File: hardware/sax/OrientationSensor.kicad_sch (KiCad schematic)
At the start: 9 parts, among them U1401 BMM150, U1402 BHI160

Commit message: Update library
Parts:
- C1401: footprint Capacitor_SMD:C_0603_1608Metric -> V2_Capacitor_SMD:C_0603; symbol Device:C_Small -> V2_Device:C_0603_10u; Manufacturer (none) -> TDK; Mouser (none) -> 810-C1608X6S1A106M; Product (none) -> C1608X6S1A106M080AC
- C1403: footprint Capacitor_SMD:C_0603_1608Metric -> V2_Capacitor_SMD:C_0603; symbol Device:C_Small -> V2_Device:C_0603_0u1; Manufacturer (none) -> TDK; Mouser (none) -> 810-CGA3E2X7R1H104MA; Product (none) -> CGA3E2X7R1H104M080AA
- C1404: footprint Capacitor_SMD:C_0603_1608Metric -> V2_Capacitor_SMD:C_0603; symbol Device:C_Small -> V2_Device:C_0603_0u47; Manufacturer (none) -> YAGEO; Mouser (none) -> 603-CC0603JR6BB474; Product (none) -> CC0603JRX7R6BB474
- R1402, R1403, R1405, R1406: footprint Resistor_SMD:R_0603_1608Metric -> V2_Resistor_SMD:R_0603; symbol Device:R_Small -> V2_Device:R_0603_2k7; Manufacturer (none) -> Vishay; Mouser (none) -> 71-CRCW06032K70FKEAC; Product (none) -> CRCW06032K70FKEAC; Rating (none) -> 100mW
- U1401: LCSC (none) -> C171681; Manufacturer (none) -> Bosch; Product (none) -> BMM150
- U1402: LCSC (none) -> C464452; Manufacturer (none) -> Bosch; Product (none) -> BHI160B
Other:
- moved on the sheet: R1402, R1403

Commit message: Replace Order_Number
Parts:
- C1401: Rating (none) -> 10V
- C1403: Rating (none) -> 50V
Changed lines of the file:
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@@
+			)
+		)
+		(property "Rating" "10V"
+			(at 130.81 113.03 0)
+			(effects
+				(font
+					(size 1.27 1.27)
+				)
+				(hide yes)
 			)
 		)
@@
 			)
 		)
-		(property "Description" "Power symbol creates a global label with name \"+3V3\""
+		(property "Description" ""
 			(at 95.25 91.44 0)
 			(effects
@@
 			)
 		)
-		(property "Description" "Power symbol creates a global label with name \"+3V3\""
+		(property "Description" ""
 			(at 125.73 85.09 0)
 			(effects
@@
 			)
 		)
-		(property "Description" "Power symbol creates a global label with name \"GND\" , ground"
+		(property "Description" ""
 			(at 133.35 105.41 0)
 			(effects
@@
 			)
 		)
-		(property "Description" "Power symbol creates a global label with name \"GND\" , ground"
+		(property "Description" ""
 			(at 209.55 114.3 0)
 			(effects
@@
 			)
 		)
+		(property "Rating" "50V"
+			(at 214.63 124.46 0)
+			(effects
+				(font
+					(size 1.27 1.27)
+				)
+				(hide yes)
+			)
+		)
 		(pin "1"
 		)
@@
 			)
 		)
-		(property "Description" "Power symbol creates a global label with name \"GND\" , ground"
+		(property "Description" ""
 			(at 214.63 102.87 0)
 			(effects
@@
 			)
 		)
-		(property "Description" "Power symbol creates a global label with name \"GND\" , ground"
+		(property "Description" ""
 			(at 130.81 90.17 0)
 			(effects
@@
 			)
 		)
-		(property "Description" "Power symbol creates a global label with name \"+3V3\""
+		(property "Description" ""
 			(at 151.13 101.6 0)
 			(effects
@@
 			)
 		)
-		(property "Description" "Power symbol creates a global label with name \"+3V3\""
+		(property "Description" ""
 			(at 191.77 114.3 0)
 			(effects
@@
 			)
 		)
-		(property "Description" "Power symbol creates a global label with name \"GND\" , ground"
+		(property "Description" ""
 			(at 191.77 106.68 0)
 			(effects
@@
 			)
 		)
-		(property "Description" "Power symbol creates a global label with name \"GND\" , ground"
+		(property "Description" ""
 			(at 191.77 101.6 0)
 			(effects
@@
 			)
 		)
-		(property "Description" "Power symbol creates a global label with name \"+3V3\""
+		(property "Description" ""
 			(at 214.63 99.06 0)
 			(effects
@@
 			)
 		)
-		(property "Description" "Power symbol creates a global label with name \"GND\" , ground"
+		(property "Description" ""
 			(at 105.41 115.57 0)
 			(effects
@@
 			)
 		)
-		(property "Description" "Power symbol creates a global label with name \"GND\" , ground"
+		(property "Description" ""
 			(at 125.73 120.65 0)
 			(effects

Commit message: Update Library
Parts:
- C1401: symbol V2_Device:C_0603_10u -> V2_Capacitor:0603_10u
- C1403: symbol V2_Device:C_0603_0u1 -> V2_Capacitor:0603_0u1
- C1404: symbol V2_Device:C_0603_0u47 -> V2_Capacitor:0603_0u47
- R1402, R1403, R1405, R1406: symbol V2_Device:R_0603_2k7 -> V2_Resistor:0603_2k7
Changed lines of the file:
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@@
 	)
 	(symbol
-		(lib_id "V2_Device:C_0603_10u")
+		(lib_id "V2_Capacitor:0603_10u")
 		(at 130.81 87.63 0)
 		(unit 1)
@@
 	)
 	(symbol
-		(lib_id "V2_Device:R_0603_2k7")
+		(lib_id "V2_Resistor:0603_2k7")
 		(at 96.52 93.98 0)
 		(unit 1)
@@
 		(on_board yes)
 		(dnp no)
-		(property "Reference" "#PWR01403"
+		(property "Reference" "#PWR1403"
 			(at 95.25 95.25 0)
 			(effects
@@
 			(project "sax"
 				(path "/6c8448b4-b04d-47e1-934e-e40cbe27a7be/f7096e67-1c66-4074-b306-32741be5ff9b"
-					(reference "#PWR01403")
-					(unit 1)
-				)
-			)
-		)
-	)
-	(symbol
-		(lib_id "V2_Device:R_0603_2k7")
+					(reference "#PWR1403")
+					(unit 1)
+				)
+			)
+		)
+	)
+	(symbol
+		(lib_id "V2_Resistor:0603_2k7")
 		(at 149.86 104.14 0)
 		(unit 1)
@@
 	)
 	(symbol
-		(lib_id "V2_Device:R_0603_2k7")
+		(lib_id "V2_Resistor:0603_2k7")
 		(at 93.98 93.98 0)
 		(unit 1)
@@
 		(on_board yes)
 		(dnp no)
-		(property "Reference" "#PWR01401"
+		(property "Reference" "#PWR1401"
 			(at 125.73 88.9 0)
 			(effects
@@
 			(project "sax"
 				(path "/6c8448b4-b04d-47e1-934e-e40cbe27a7be/f7096e67-1c66-4074-b306-32741be5ff9b"
-					(reference "#PWR01401")
+					(reference "#PWR1401")
 					(unit 1)
 				)
@@
 		(on_board yes)
 		(dnp no)
-		(property "Reference" "#PWR01411"
+		(property "Reference" "#PWR1411"
 			(at 139.7 105.41 0)
 			(effects
@@
 			(project "sax"
 				(path "/6c8448b4-b04d-47e1-934e-e40cbe27a7be/f7096e67-1c66-4074-b306-32741be5ff9b"
-					(reference "#PWR01411")
+					(reference "#PWR1411")
 					(unit 1)
 				)
@@
 		(on_board yes)
 		(dnp no)
-		(property "Reference" "#PWR01414"
+		(property "Reference" "#PWR1414"
 			(at 215.9 114.3 0)
 			(effects
@@
 			(project "sax"
 				(path "/6c8448b4-b04d-47e1-934e-e40cbe27a7be/f7096e67-1c66-4074-b306-32741be5ff9b"
-					(reference "#PWR01414")
-					(unit 1)
-				)
-			)
-		)
-	)
-	(symbol
-		(lib_id "V2_Device:C_0603_0u1")
+					(reference "#PWR1414")
+					(unit 1)
+				)
+			)
+		)
+	)
+	(symbol
+		(lib_id "V2_Capacitor:0603_0u1")
 		(at 214.63 101.6 0)
 		(unit 1)
@@
 		(on_board yes)
 		(dnp no)
-		(property "Reference" "#PWR01410"
+		(property "Reference" "#PWR1410"
 			(at 214.63 109.22 0)
 			(effects
@@
 			(project "sax"
 				(path "/6c8448b4-b04d-47e1-934e-e40cbe27a7be/f7096e67-1c66-4074-b306-32741be5ff9b"
-					(reference "#PWR01410")
+					(reference "#PWR1410")
 					(unit 1)
 				)
@@
 		(on_board yes)
 		(dnp no)
-		(property "Reference" "#PWR01402"
+		(property "Reference" "#PWR1402"
 			(at 130.81 96.52 0)
 			(effects
@@
 			(project "sax"
 				(path "/6c8448b4-b04d-47e1-934e-e40cbe27a7be/f7096e67-1c66-4074-b306-32741be5ff9b"
-					(reference "#PWR01402")
+					(reference "#PWR1402")
 					(unit 1)
 				)
@@
 		(on_board yes)
 		(dnp no)
-		(property "Reference" "#PWR01408"
+		(property "Reference" "#PWR1408"
 			(at 151.13 105.41 0)
 			(effects
@@
 			(project "sax"
 				(path "/6c8448b4-b04d-47e1-934e-e40cbe27a7be/f7096e67-1c66-4074-b306-32741be5ff9b"
-					(reference "#PWR01408")
+					(reference "#PWR1408")
 					(unit 1)
 				)
@@
 	)
 	(symbol
-		(lib_id "V2_Device:C_0603_0u47")
+		(lib_id "V2_Capacitor:0603_0u47")
 		(at 130.81 105.41 90)
 		(unit 1)
@@
 		(on_board yes)
 		(dnp no)
-		(property "Reference" "#PWR01413"
+		(property "Reference" "#PWR1413"
 			(at 195.58 114.3 0)
 			(effects
@@
 			(project "sax"
 				(path "/6c8448b4-b04d-47e1-934e-e40cbe27a7be/f7096e67-1c66-4074-b306-32741be5ff9b"
-					(reference "#PWR01413")
+					(reference "#PWR1413")
 					(unit 1)
 				)
@@
 		(on_board yes)
 		(dnp no)
-		(property "Reference" "#PWR01412"
+		(property "Reference" "#PWR1412"
 			(at 185.42 106.68 0)
 			(effects
@@
 			(project "sax"
 				(path "/6c8448b4-b04d-47e1-934e-e40cbe27a7be/f7096e67-1c66-4074-b306-32741be5ff9b"
-					(reference "#PWR01412")
+					(reference "#PWR1412")
 					(unit 1)
 				)
@@
 		(on_board yes)
 		(dnp no)
-		(property "Reference" "#PWR01409"
+		(property "Reference" "#PWR1409"
 			(at 185.42 101.6 0)
 			(effects
@@
 			(project "sax"
 				(path "/6c8448b4-b04d-47e1-934e-e40cbe27a7be/f7096e67-1c66-4074-b306-32741be5ff9b"
-					(reference "#PWR01409")
+					(reference "#PWR1409")
 					(unit 1)
 				)
@@
 		(on_board yes)
 		(dnp no)
-		(property "Reference" "#PWR01406"
+		(property "Reference" "#PWR1406"
 			(at 214.63 102.87 0)
 			(effects
@@
 			(project "sax"
 				(path "/6c8448b4-b04d-47e1-934e-e40cbe27a7be/f7096e67-1c66-4074-b306-32741be5ff9b"
-					(reference "#PWR01406")
+					(reference "#PWR1406")
 					(unit 1)
 				)
@@
 		(on_board yes)
 		(dnp no)
-		(property "Reference" "#PWR01415"
+		(property "Reference" "#PWR1415"
 			(at 99.06 115.57 0)
 			(effects
@@
 			(project "sax"
 				(path "/6c8448b4-b04d-47e1-934e-e40cbe27a7be/f7096e67-1c66-4074-b306-32741be5ff9b"
-					(reference "#PWR01415")
+					(reference "#PWR1415")
 					(unit 1)
 				)
@@
 	)
 	(symbol
-		(lib_id "V2_Device:R_0603_2k7")
+		(lib_id "V2_Resistor:0603_2k7")
 		(at 152.4 104.14 0)
 		(unit 1)
@@
 		(on_board yes)
 		(dnp no)
-		(property "Reference" "#PWR01416"
+		(property "Reference" "#PWR1416"
 			(at 132.08 120.65 0)
 			(effects
@@
 			(project "sax"
 				(path "/6c8448b4-b04d-47e1-934e-e40cbe27a7be/f7096e67-1c66-4074-b306-32741be5ff9b"
-					(reference "#PWR01416")
-					(unit 1)
-				)
+					(reference "#PWR1416")
+					(unit 1)
+				)

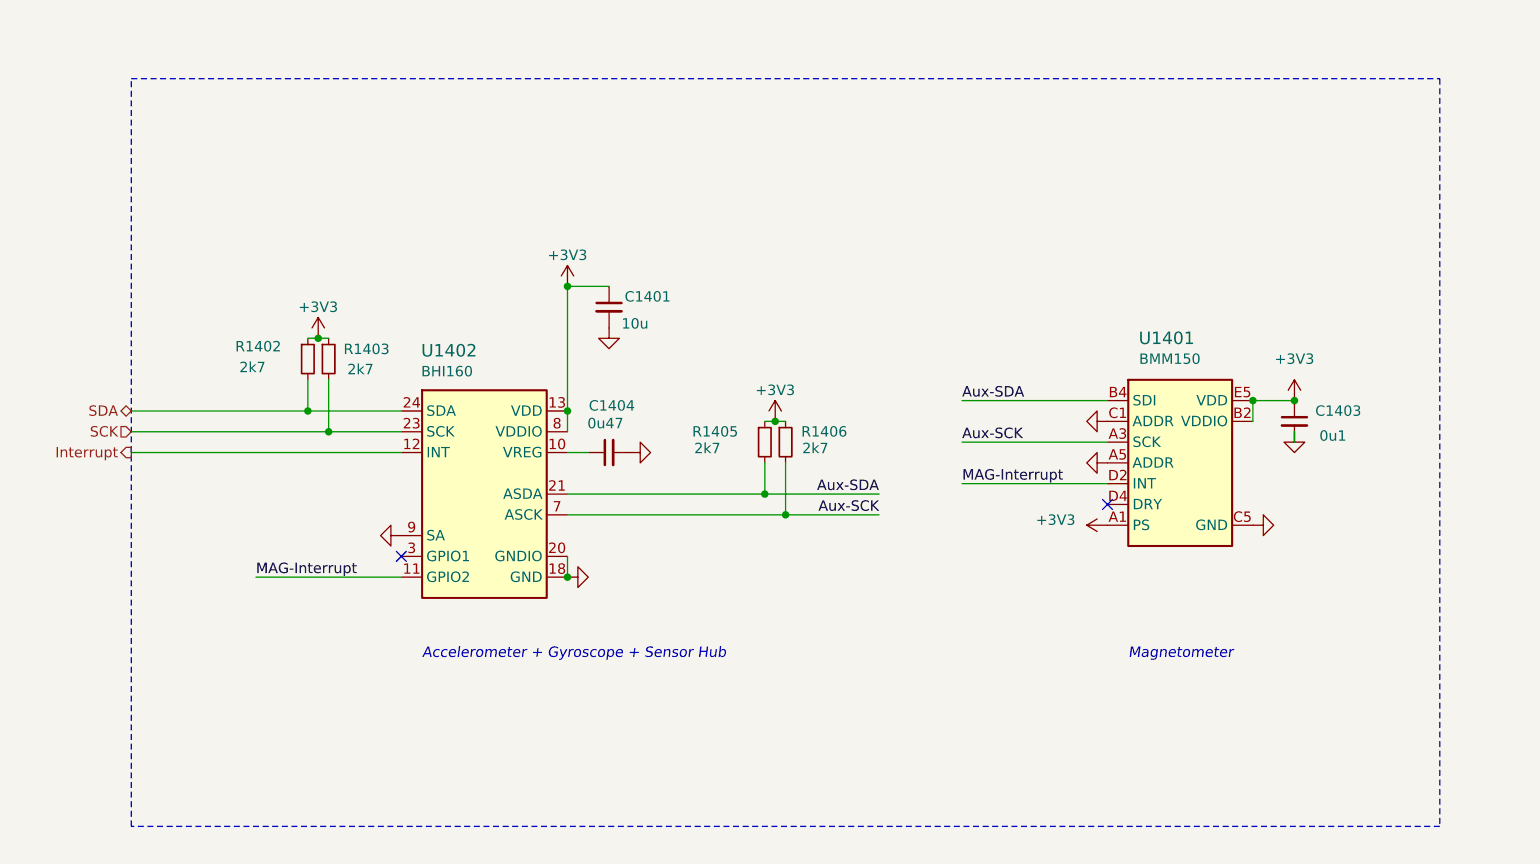
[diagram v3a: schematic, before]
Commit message: sax2 -> sax
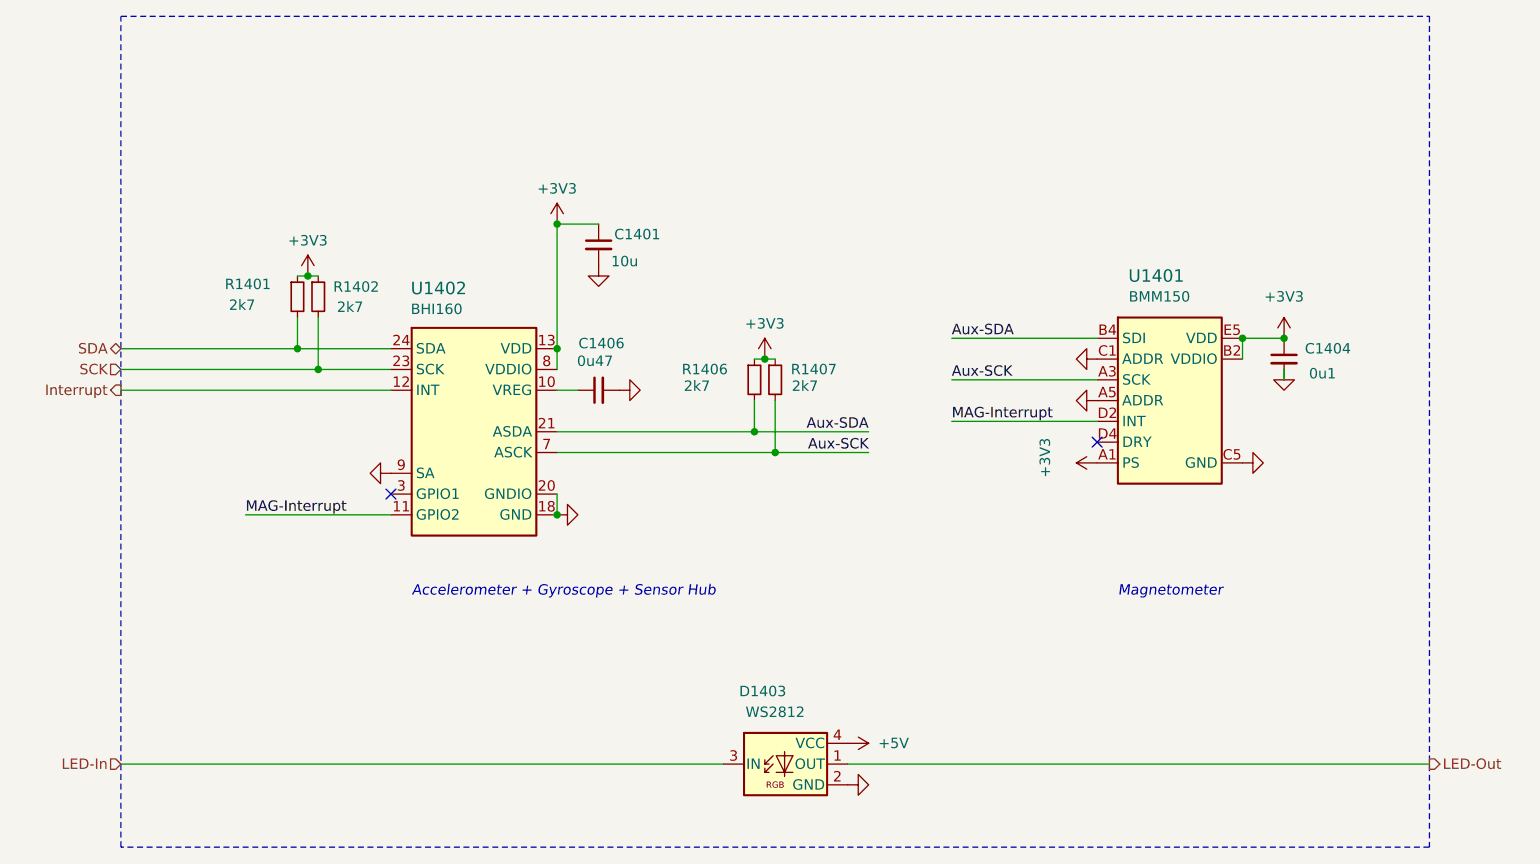
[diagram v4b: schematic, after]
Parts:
- added D1403: WS2812, V2_LED:WS2812-2020, symbol V2_LED:WS2812
- renumbered C1403 to C1404, C1404 to C1406, R1402 to R1401, R1403 to R1402, R1405 to R1406, R1406 to R1407
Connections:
- net GND: now also D1403.2 (GND)
- new net +5V: D1403.4 (VCC)
- new net LED-In: D1403.3 (IN)
- new net LED-Out: D1403.1 (OUT)
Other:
- moved on the sheet: C1401, C1404, C1406, R1401, R1402, R1406, R1407, U1401, U1402

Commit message: KiCad 10
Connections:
- net Aux-SCK renamed Aux-SCL
- net SCK renamed SCL

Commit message: Replace step-down
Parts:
- C1406: Manufacturer YAGEO -> TDK; Mouser 603-CC0603JR6BB474 -> 810-CGA3E3X7R1H474KB; Product CC0603JRX7R6BB474 -> CGA3E3X7R1H474K080AB; Rating (none) -> 50V
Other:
- title: Orientation Sensor -> V2 sax
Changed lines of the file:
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@@
 	(paper "A4")
 	(title_block
-		(title "Orientation Sensor")
-		(date "2026-03-21")
-		(rev "2026-02-10")
+		(title "V2 sax")
+		(date "2026-03-31")
+		(rev "2026-03-31")
 		(company "Versio Duo")
 	)
@@
 			)
 		)
-		(property "Mouser" "603-CC0603JR6BB474"
+		(property "Mouser" "810-CGA3E3X7R1H474KB"
 			(at 149.86 97.79 0)
 			(hide yes)
@@
 			)
 		)
-		(property "Product" "CC0603JRX7R6BB474"
+		(property "Product" "CGA3E3X7R1H474K080AB"
 			(at 147.32 97.79 0)
 			(hide yes)
@@
 			)
 		)
-		(property "Manufacturer" "YAGEO"
+		(property "Manufacturer" "TDK"
 			(at 144.78 97.79 0)
 			(hide yes)
 			(show_name no)
+			(do_not_autoplace no)
+			(effects
+				(font
+					(size 1.27 1.27)
+				)
+			)
+		)
+		(property "Rating" "50V"
+			(at 152.4 97.79 0)
+			(hide yes)
+			(show_name no)
